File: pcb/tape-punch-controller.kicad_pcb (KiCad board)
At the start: 2 copper layers, 70 x 88 mm, 148 parts, among them J1 Conn_01x06, J2 Conn_01x09, J3 USB_B, J4 Conn_01x16, J5 Conn_01x06, J6 Conn_01x02, J7 Conn_02x03_Odd_Even, J8 Conn_01x04, Q1 IRLML0060, Q10 IRLML0060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

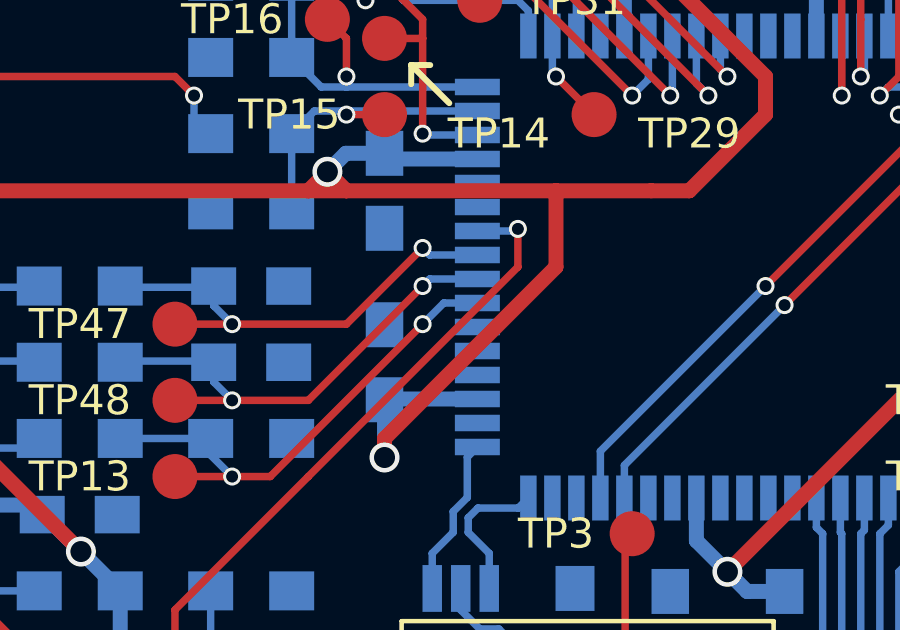
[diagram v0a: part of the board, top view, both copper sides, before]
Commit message: pcb: fix SYNC being wired to wrong pin (should be PE2, not PE3)
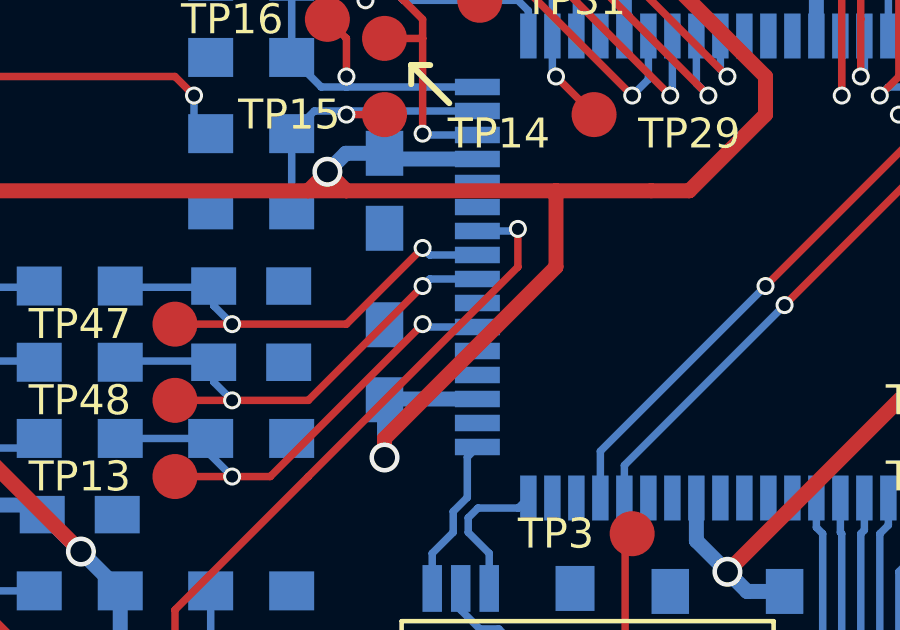
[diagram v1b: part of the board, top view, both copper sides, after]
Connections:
- U1 pad 38: GND -> SYNC
- U1 pad 39: SYNC -> GND
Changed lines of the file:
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@@
     (links 278)
     (no_connects 0)
-    (area 89.371428 18 164.628573 110.000001)
+    (area 91.949999 19.949999 162.050001 108.050001)
     (thickness 1.6)
     (drawings 76)
@@
       (net 2 GND))
     (pad 38 smd rect (at 7.7 -2 180) (size 1.5 0.55) (layers B.Cu B.Paste B.Mask)
-      (net 2 GND))
-    (pad 39 smd rect (at 7.7 -1.2 180) (size 1.5 0.55) (layers B.Cu B.Paste B.Mask)
       (net 69 SYNC))
+    (pad 39 smd rect (at 7.7 -1.2 180) (size 1.5 0.55) (layers B.Cu B.Paste B.Mask)
+      (net 2 GND))
     (pad 40 smd rect (at 7.7 -0.4 180) (size 1.5 0.55) (layers B.Cu B.Paste B.Mask)
       (net 7 NO_TAPE))
@@
   (segment (start 118.745 92.075) (end 118.745 94.615) (width 0.25) (layer F.Cu) (net 68))
   (segment (start 111.76 102.155) (end 111.76 97.87) (width 0.25) (layer B.Cu) (net 68))
+  (segment (start 128.825 82.645) (end 127.095 82.645) (width 0.25) (layer B.Cu) (net 69))
+  (segment (start 127.095 82.645) (end 127 82.55) (width 0.25) (layer B.Cu) (net 69))
   (segment (start 118.745 87.63) (end 120.65 87.63) (width 0.25) (layer F.Cu) (net 69))
-  (segment (start 128.825 81.845) (end 127.705 81.845) (width 0.25) (layer B.Cu) (net 69))
-  (segment (start 127.705 81.845) (end 127 82.55) (width 0.25) (layer B.Cu) (net 69))
   (segment (start 127 82.55) (end 121.92 87.63) (width 0.25) (layer F.Cu) (net 69))
   (segment (start 121.92 87.63) (end 120.65 87.63) (width 0.25) (layer F.Cu) (net 69))
